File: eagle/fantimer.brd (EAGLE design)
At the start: 58 x 78 mm, 16 parts, among them IC1 PIC10F200, K1 PB2032-ND, Q1 2N7000-G, U1 IRM-01-5, X1 732-10957-ND

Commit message: Pulldown 100k. Fix up diodes, resistors and filter cap in BOM.
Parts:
- R4: value 10k -> 100k
- renumbered D3 to D2
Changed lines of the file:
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@@
 </element>
 <element name="R2" library="resistor" library_urn="urn:adsk.eagle:library:348" package="0207/7" package3d_urn="urn:adsk.eagle:package:25942/1" value="1.6k" x="29.21" y="7.62"/>
-<element name="D3" library="diode" library_urn="urn:adsk.eagle:library:210" package="CB417-15" package3d_urn="urn:adsk.eagle:package:43349/1" value="P6KE91CA" x="20.32" y="0"/>
+<element name="D2" library="diode" library_urn="urn:adsk.eagle:library:210" package="CB417-15" package3d_urn="urn:adsk.eagle:package:43349/1" value="P6KE91CA" x="20.32" y="0"/>
 <element name="C1" library="rcl" library_urn="urn:adsk.eagle:library:334" package="C102-064X133" package3d_urn="urn:adsk.eagle:package:23653/1" value="330nF" x="2.54" y="10.16" rot="R270">
 <attribute name="SPICEPREFIX" value="C" x="2.54" y="10.16" size="1.778" layer="27" rot="R270" display="off"/>
@@
 </element>
 <element name="IC1" library="microchip-addl" package="DIL08" package3d_urn="urn:adsk.eagle:package:14440/1" value="PIC10F200" x="45.72" y="25.4" rot="R270"/>
-<element name="R4" library="resistor" library_urn="urn:adsk.eagle:library:348" package="0207/7" package3d_urn="urn:adsk.eagle:package:25942/1" value="10k" x="38.1" y="43.18" rot="R270"/>
+<element name="R4" library="resistor" library_urn="urn:adsk.eagle:library:348" package="0207/7" package3d_urn="urn:adsk.eagle:package:25942/1" value="100k" x="38.1" y="43.18" rot="R270"/>
 <element name="C4" library="rcl" library_urn="urn:adsk.eagle:library:334" package="C025-025X050" package3d_urn="urn:adsk.eagle:package:23629/2" value="1uF" x="45.72" y="38.1">
 <attribute name="SPICEPREFIX" value="C" x="45.72" y="38.1" size="1.778" layer="27" display="off"/>
@@
 <contactref element="U1" pad="AC/N"/>
 <contactref element="OK1" pad="2"/>
-<contactref element="D3" pad="A"/>
+<contactref element="D2" pad="A"/>
 <wire x1="2.54" y1="37.853" x2="2.48" y2="45.74" width="0" layer="19" extent="1-1"/>
 <wire x1="27.94" y1="0" x2="2.54" y2="37.853" width="0" layer="19" extent="1-1"/>
@@
 </signal>
 <signal name="VZ">
-<contactref element="D3" pad="C"/>
+<contactref element="D2" pad="C"/>
 <contactref element="C2" pad="1"/>
 <contactref element="R1" pad="2"/>

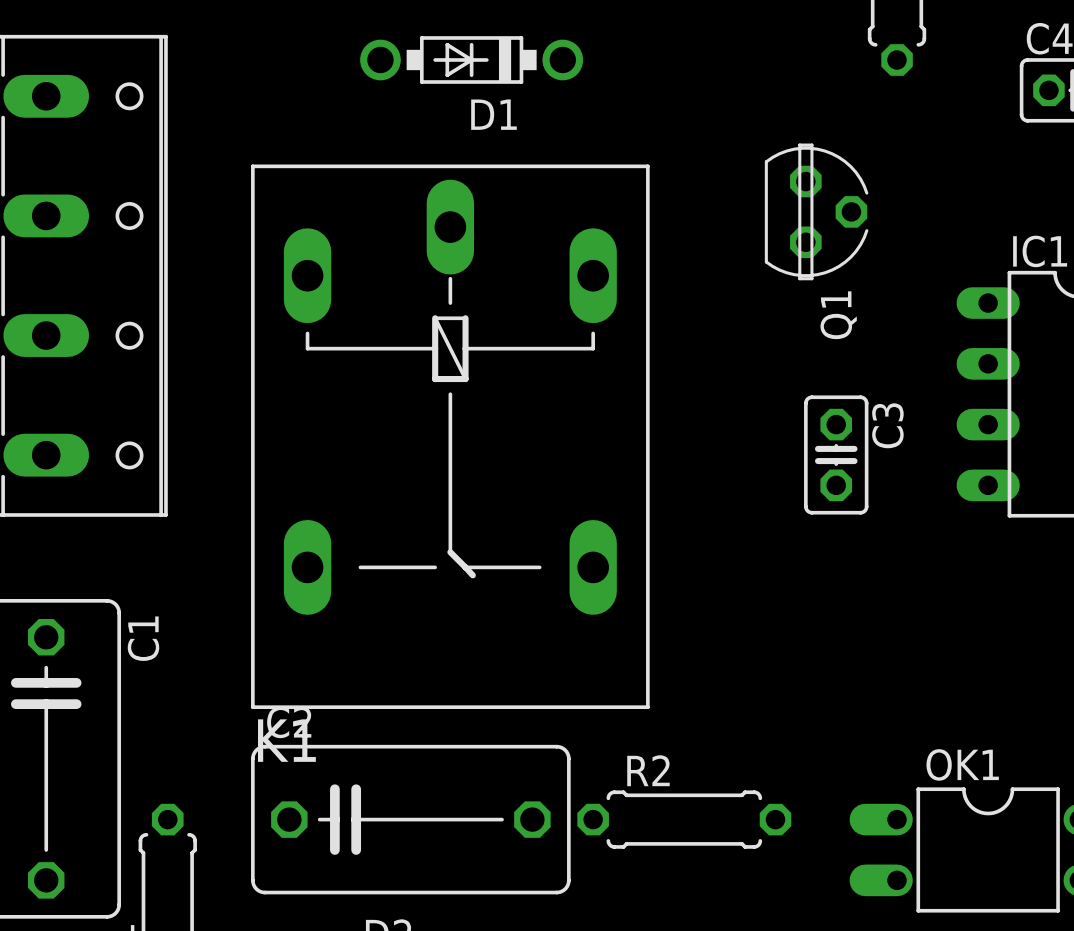
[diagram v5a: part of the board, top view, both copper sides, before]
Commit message: Replace TVS with varistor across relay
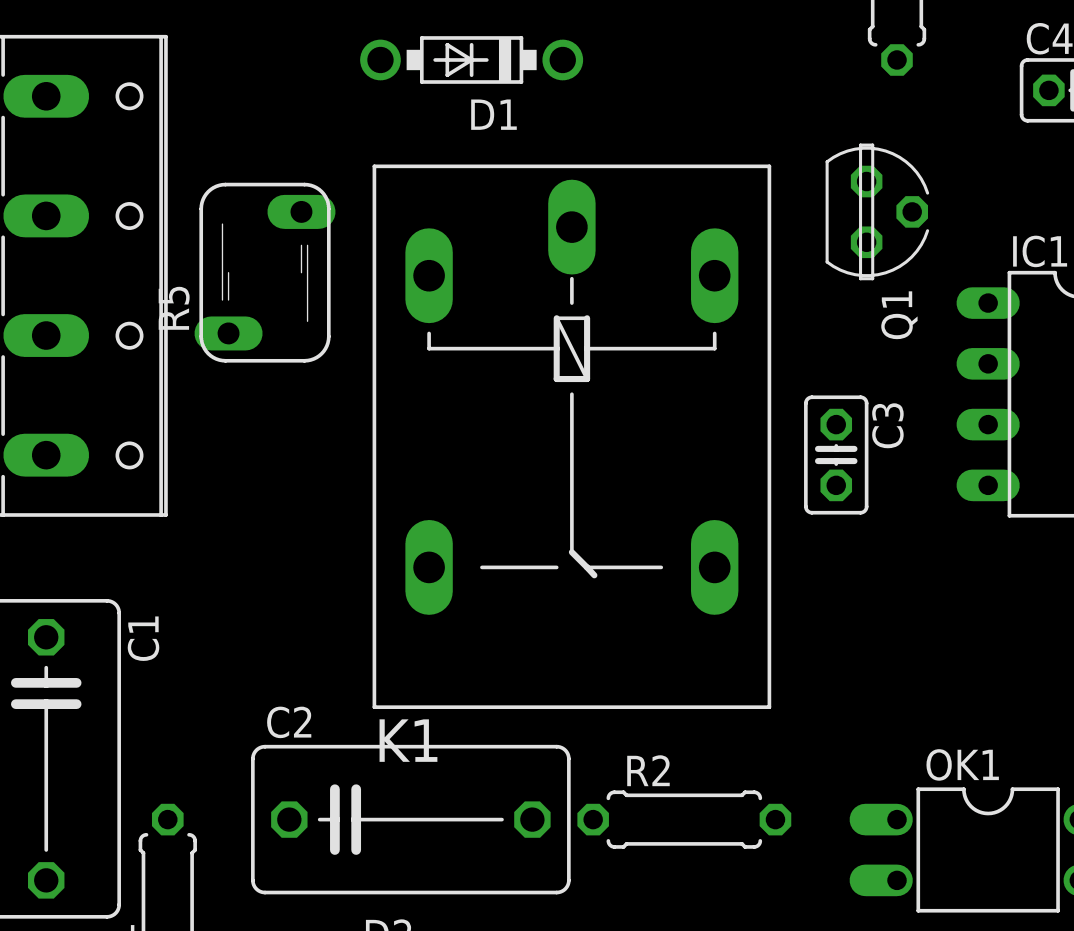
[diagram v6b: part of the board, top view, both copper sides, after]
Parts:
- added R5: MOV-07D201K, varistor:S05K300
- moved K1 5.08 mm to (24.5, 22.9)
- moved Q1 2.54 mm to (36.8, 33.0)
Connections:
- net AC/N: now also R5.2
- net LIVE_FAN: now also R5.1
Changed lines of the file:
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@@
 <attribute name="VALUE" x="-1.2192" y="38.0054" size="1.27" layer="27" ratio="10" rot="R270"/>
 </element>
-<element name="Q1" library="transistor-fet" library_urn="urn:adsk.eagle:library:396" package="TO237" package3d_urn="urn:adsk.eagle:package:28531/2" value="2N7000-G" x="34.29" y="33.02" rot="R270"/>
-<element name="K1" library="relay" library_urn="urn:adsk.eagle:library:339" package="G5LE" package3d_urn="urn:adsk.eagle:package:24308/1" value="PB2032-ND" x="19.431" y="22.86" rot="R270">
-<attribute name="MF" value="" x="19.431" y="22.86" size="1.778" layer="27" rot="R270" display="off"/>
-<attribute name="MPN" value="" x="19.431" y="22.86" size="1.778" layer="27" rot="R270" display="off"/>
-<attribute name="OC_FARNELL" value="unknown" x="19.431" y="22.86" size="1.778" layer="27" rot="R270" display="off"/>
-<attribute name="OC_NEWARK" value="unknown" x="19.431" y="22.86" size="1.778" layer="27" rot="R270" display="off"/>
+<element name="Q1" library="transistor-fet" library_urn="urn:adsk.eagle:library:396" package="TO237" package3d_urn="urn:adsk.eagle:package:28531/2" value="2N7000-G" x="36.83" y="33.02" rot="R270"/>
+<element name="K1" library="relay" library_urn="urn:adsk.eagle:library:339" package="G5LE" package3d_urn="urn:adsk.eagle:package:24308/1" value="PB2032-ND" x="24.511" y="22.86" rot="R270">
+<attribute name="MF" value="" x="24.511" y="22.86" size="1.778" layer="27" rot="R270" display="off"/>
+<attribute name="MPN" value="" x="24.511" y="22.86" size="1.778" layer="27" rot="R270" display="off"/>
+<attribute name="OC_FARNELL" value="unknown" x="24.511" y="22.86" size="1.778" layer="27" rot="R270" display="off"/>
+<attribute name="OC_NEWARK" value="unknown" x="24.511" y="22.86" size="1.778" layer="27" rot="R270" display="off"/>
 </element>
 <element name="D1" library="diode" library_urn="urn:adsk.eagle:library:210" package="DO41-7.6" package3d_urn="urn:adsk.eagle:package:43421/1" value="SB140TA" x="20.32" y="39.37" rot="R180"/>
@@
 <attribute name="SPICEPREFIX" value="C" x="45.72" y="38.1" size="1.778" layer="27" display="off"/>
 </element>
+<element name="R5" library="varistor" library_urn="urn:adsk.eagle:library:410" package="S05K300" package3d_urn="urn:adsk.eagle:package:30536/1" value="MOV-07D201K" x="11.684" y="30.48"/>
 </elements>
 <signals>
@@
 <contactref element="OK1" pad="2"/>
 <contactref element="D2" pad="A"/>
+<contactref element="R5" pad="2"/>
 <wire x1="2.54" y1="37.853" x2="2.48" y2="45.74" width="0" layer="19" extent="1-1"/>
-<wire x1="27.94" y1="0" x2="2.54" y2="37.853" width="0" layer="19" extent="1-1"/>
+<wire x1="13.208" y1="33.02" x2="2.54" y2="37.853" width="0" layer="19" extent="1-1"/>
+<wire x1="27.94" y1="0" x2="13.208" y2="33.02" width="0" layer="19" extent="1-1"/>
 <wire x1="38.1" y1="5.08" x2="27.94" y2="0" width="0" layer="19" extent="1-1"/>
 </signal>
@@
 <contactref element="U1" pad="AC/L"/>
 <wire x1="2.54" y1="32.853" x2="2.48" y2="60.94" width="0" layer="19" extent="1-1"/>
-<wire x1="13.462" y1="18.161" x2="2.54" y2="32.853" width="0" layer="19" extent="1-1"/>
+<wire x1="18.542" y1="18.161" x2="2.54" y2="32.853" width="0" layer="19" extent="1-1"/>
 </signal>
 <signal name="LIVE_FAN">
 <contactref element="X1" pad="3"/>
 <contactref element="K1" pad="P"/>
-<wire x1="2.54" y1="27.853" x2="19.431" y2="32.385" width="0" layer="19" extent="1-1"/>
+<contactref element="R5" pad="1"/>
+<wire x1="10.16" y1="27.94" x2="24.511" y2="32.385" width="0" layer="19" extent="1-1"/>
+<wire x1="2.54" y1="27.853" x2="10.16" y2="27.94" width="0" layer="19" extent="1-1"/>
 </signal>
 <signal name="LIVE_LIGHT">
@@
 <contactref element="IC1" pad="3"/>
 <contactref element="R4" pad="2"/>
-<wire x1="36.195" y1="33.02" x2="38.1" y2="39.37" width="0" layer="19" extent="1-1"/>
-<wire x1="41.91" y1="24.13" x2="36.195" y2="33.02" width="0" layer="19" extent="1-1"/>
+<wire x1="38.735" y1="33.02" x2="38.1" y2="39.37" width="0" layer="19" extent="1-1"/>
+<wire x1="41.91" y1="24.13" x2="38.735" y2="33.02" width="0" layer="19" extent="1-1"/>
 </signal>
 <signal name="COILOUT">
@@
 <contactref element="K1" pad="1"/>
 <contactref element="D1" pad="A"/>
-<wire x1="16.51" y1="39.37" x2="34.29" y2="31.75" width="0" layer="19" extent="1-1"/>
-<wire x1="13.462" y1="30.353" x2="16.51" y2="39.37" width="0" layer="19" extent="1-1"/>
+<wire x1="18.542" y1="30.353" x2="36.83" y2="31.75" width="0" layer="19" extent="1-1"/>
+<wire x1="16.51" y1="39.37" x2="18.542" y2="30.353" width="0" layer="19" extent="1-1"/>
 </signal>
 <signal name="!LIGHT">
@@
 <wire x1="38.1" y1="46.99" x2="43.18" y2="50.8" width="0" layer="19" extent="1-1"/>
 <wire x1="30.48" y1="45.74" x2="38.1" y2="46.99" width="0" layer="19" extent="1-1"/>
-<wire x1="34.29" y1="34.29" x2="30.48" y2="45.74" width="0" layer="19" extent="1-1"/>
+<wire x1="36.83" y1="34.29" x2="30.48" y2="45.74" width="0" layer="19" extent="1-1"/>
 <wire x1="46.99" y1="38.1" x2="38.1" y2="46.99" width="0" layer="19" extent="1-1"/>
 <wire x1="49.53" y1="26.67" x2="46.99" y2="38.1" width="0" layer="19" extent="1-1"/>
@@
 <wire x1="30.48" y1="53.34" x2="43.18" y2="55.88" width="0" layer="19" extent="1-1"/>
 <wire x1="24.13" y1="39.37" x2="30.48" y2="53.34" width="0" layer="19" extent="1-1"/>
-<wire x1="25.4" y1="30.353" x2="24.13" y2="39.37" width="0" layer="19" extent="1-1"/>
-<wire x1="35.56" y1="24.13" x2="25.4" y2="30.353" width="0" layer="19" extent="1-1"/>
+<wire x1="30.48" y1="30.353" x2="24.13" y2="39.37" width="0" layer="19" extent="1-1"/>
+<wire x1="35.56" y1="24.13" x2="30.48" y2="30.353" width="0" layer="19" extent="1-1"/>
 <wire x1="41.91" y1="26.67" x2="35.56" y2="24.13" width="0" layer="19" extent="1-1"/>
 <wire x1="44.45" y1="38.1" x2="41.91" y2="26.67" width="0" layer="19" extent="1-1"/>

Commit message: Library updates
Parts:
- IC1: value PIC10F200 -> PIC10F220
- U1: device meanwell:IRM02-PCB -> meanwell:IRM-01-X
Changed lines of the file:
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@@
 </element>
 <element name="D1" library="diode" library_urn="urn:adsk.eagle:library:210" package="DO41-7.6" package3d_urn="urn:adsk.eagle:package:43421/1" value="SB140TA" x="20.32" y="39.37" rot="R180"/>
-<element name="U1" library="meanwell" package="IRM02-PCB" value="IRM-01-5" x="30.48" y="53.34" rot="R180"/>
+<element name="U1" library="meanwell" package="IRM-01-X" value="IRM-01-5" x="30.48" y="53.34" rot="R180"/>
 <element name="OK1" library="optocoupler" library_urn="urn:adsk.eagle:library:320" package="DIL04" package3d_urn="urn:adsk.eagle:package:21938/1" value="LTV814H" x="41.91" y="6.35" rot="R270">
 <attribute name="MF" value="" x="41.91" y="6.35" size="1.778" layer="27" rot="R270" display="off"/>
@@
 <attribute name="OC_NEWARK" value="unknown" x="41.91" y="6.35" size="1.778" layer="27" rot="R270" display="off"/>
 </element>
-<element name="R2" library="resistor" library_urn="urn:adsk.eagle:library:348" package="0207/7" package3d_urn="urn:adsk.eagle:package:25942/1" value="1.6k" x="29.21" y="7.62"/>
+<element name="R2" library="resistor" library_urn="urn:adsk.eagle:library:348" package="0207/7" package3d_urn="urn:adsk.eagle:package:23493/1" value="1.6k" x="29.21" y="7.62"/>
 <element name="D2" library="diode" library_urn="urn:adsk.eagle:library:210" package="CB417-15" package3d_urn="urn:adsk.eagle:package:43349/1" value="P6KE91CA" x="20.32" y="0"/>
 <element name="C1" library="rcl" library_urn="urn:adsk.eagle:library:334" package="C102-064X133" package3d_urn="urn:adsk.eagle:package:23653/1" value="330nF" x="2.54" y="10.16" rot="R270">
@@
 <attribute name="SPICEPREFIX" value="C" x="17.78" y="7.62" size="1.778" layer="27" display="off"/>
 </element>
-<element name="R1" library="resistor" library_urn="urn:adsk.eagle:library:348" package="0207/7" package3d_urn="urn:adsk.eagle:package:25942/1" value="1.6k" x="7.62" y="3.81" rot="R90"/>
+<element name="R1" library="resistor" library_urn="urn:adsk.eagle:library:348" package="0207/7" package3d_urn="urn:adsk.eagle:package:23493/1" value="1.6k" x="7.62" y="3.81" rot="R90"/>
 <element name="R3" library="rcl" library_urn="urn:adsk.eagle:library:334" package="PT-10" package3d_urn="urn:adsk.eagle:package:23786/1" value="4.7k" x="48.26" y="53.34" rot="R270">
 <attribute name="SPICEMODEL" value="POT" x="48.26" y="53.34" size="1.778" layer="27" rot="R270" display="off"/>
@@
 <attribute name="SPICEPREFIX" value="C" x="35.56" y="22.86" size="1.778" layer="27" rot="R270" display="off"/>
 </element>
-<element name="IC1" library="microchip-addl" package="DIL08" package3d_urn="urn:adsk.eagle:package:14440/1" value="PIC10F200" x="45.72" y="25.4" rot="R270"/>
-<element name="R4" library="resistor" library_urn="urn:adsk.eagle:library:348" package="0207/7" package3d_urn="urn:adsk.eagle:package:25942/1" value="100k" x="38.1" y="43.18" rot="R270"/>
+<element name="IC1" library="microchip-addl" package="DIL08" package3d_urn="urn:adsk.eagle:package:14440/1" value="PIC10F220" x="45.72" y="25.4" rot="R270"/>
+<element name="R4" library="resistor" library_urn="urn:adsk.eagle:library:348" package="0207/7" package3d_urn="urn:adsk.eagle:package:23493/1" value="100k" x="38.1" y="43.18" rot="R270"/>
 <element name="C4" library="rcl" library_urn="urn:adsk.eagle:library:334" package="C025-025X050" package3d_urn="urn:adsk.eagle:package:23629/2" value="1uF" x="45.72" y="38.1">
 <attribute name="SPICEPREFIX" value="C" x="45.72" y="38.1" size="1.778" layer="27" display="off"/>

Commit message: Adjust detection cap based on experiment
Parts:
- C3: value 1uF -> 47nF
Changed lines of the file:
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@@
 <attribute name="SPICEPREFIX" value="X" x="48.26" y="53.34" size="1.778" layer="27" rot="R270" display="off"/>
 </element>
-<element name="C3" library="rcl" library_urn="urn:adsk.eagle:library:334" package="C025-025X050" package3d_urn="urn:adsk.eagle:package:23629/2" value="1uF" x="35.56" y="22.86" rot="R270">
+<element name="C3" library="rcl" library_urn="urn:adsk.eagle:library:334" package="C025-025X050" package3d_urn="urn:adsk.eagle:package:23629/2" value="47nF" x="35.56" y="22.86" rot="R270">
 <attribute name="SPICEPREFIX" value="C" x="35.56" y="22.86" size="1.778" layer="27" rot="R270" display="off"/>
 </element>
